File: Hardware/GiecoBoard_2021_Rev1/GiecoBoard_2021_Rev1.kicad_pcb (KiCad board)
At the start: 2 copper layers, 125.7 x 104.1 mm, 62 parts, among them J1 Conn_02x02_Top_Bottom, J10 Test_Point, J11 Conn_02x02_Top_Bottom, J2 Conn_02x02_Top_Bottom, J3 Conn_02x02_Top_Bottom, J4 Conn_02x02_Top_Bottom, J5 Conn_02x02_Top_Bottom, J6 Conn_02x02_Top_Bottom, J7 Conn_02x02_Top_Bottom, J8 Conn_02x02_Top_Bottom, J9 Conn_02x02_Top_Bottom, U1 TM4C129E_Launchpad, U2 LM2576SX-3.3

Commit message: Post CDR update
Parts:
- removed D22: 1n5582, Diode_THT:D_DO-201AD_P15.24mm_Horizontal
- removed G***: LOGO, MRDT_Silkscreens:z_sig_SanfanLiu_sig21.8mmx12.3mm1
- removed G***: LOGO, MRDT_Silkscreens:0_MRDT_Logo_7.5mm
- removed the J10 at (125.1, 88.9)
- removed L1: 100uH, Inductor_SMD:L_0603_1608Metric_Pad1.05x0.95mm_HandSolder
- C1: value 100uF -> 10uF
- C2: value 1000uF -> 10uF; moved to F.Cu
- D1, D11, D13, D14, D16, D3, D4, D6, D8, D9: value LED -> Green
- D10, D12, D15, D17, D18, D19, D2, D20, D5, D7: value LED -> Blue
- D21: value LED -> Green; moved to F.Cu
- R21: moved to F.Cu
- U2: value LM2576SX-3.3 -> OKI; footprint MRDT_Devices:LM2576 -> MRDT_Devices:OKI_Horizontal
- moved D12 74.9 mm to (219.1, 84.1)
- moved D9 74.6 mm to (154.9, 122.8)
- moved D6 43.6 mm to (194.3, 84.1)
- moved D7 42.9 mm to (179.7, 122.8)
- moved D14 42.8 mm to (154.9, 84.1)
- moved D15 42.0 mm to (160.0, 122.8)
- moved D17 42.0 mm to (142.2, 122.8)
- moved D13 39.2 mm to (137.2, 84.1)
- moved D16 38.1 mm to (175.3, 84.1)
- moved D11 22.9 mm to (137.2, 122.8)
- moved D19 19.7 mm to (160.0, 84.1)
- moved D8 19.7 mm to (214.0, 84.1)
- moved D4 19.7 mm to (174.6, 122.8)
- moved D5 19.7 mm to (199.4, 122.8)
- moved D10 14.6 mm to (199.4, 84.1)
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- renumbered J11 to J10, R2 to R1, R7 to R10, R14 to R11, R9 to R12, R16 to R13, R18 to R14, R11 to R15, R20 to R16, R13 to R17, R15 to R18, R17 to R19, R1 to R2, R19 to R20, R4 to R3, R6 to R4, R3 to R5, R8 to R6, R5 to R7, R10 to R8, R12 to R9
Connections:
- C1 pad 1: GND -> Net-(C1-Pad1)
- C1 pad 2: Net-(C1-Pad2) -> GND
- Conn1 pad 2: Net-(C1-Pad2) -> Net-(C1-Pad1)
- R1 pad 1: Net-(D2-Pad2) -> Net-(D1-Pad2)
- R10 pad 1: Net-(D7-Pad2) -> Net-(D10-Pad2)
- R11 pad 1: Net-(D14-Pad2) -> Net-(D11-Pad2)
- R12 pad 1: Net-(D9-Pad2) -> Net-(D12-Pad2)
- R13 pad 1: Net-(D16-Pad2) -> Net-(D13-Pad2)
- R14 pad 1: Net-(D18-Pad2) -> Net-(D14-Pad2)
- R15 pad 1: Net-(D11-Pad2) -> Net-(D15-Pad2)
- R16 pad 1: Net-(D20-Pad2) -> Net-(D16-Pad2)
- R17 pad 1: Net-(D13-Pad2) -> Net-(D17-Pad2)
- R18 pad 1: Net-(D15-Pad2) -> Net-(D18-Pad2)
- R19 pad 1: Net-(D17-Pad2) -> Net-(D19-Pad2)
- R2 pad 1: Net-(D1-Pad2) -> Net-(D2-Pad2)
- R20 pad 1: Net-(D19-Pad2) -> Net-(D20-Pad2)
- R3 pad 1: Net-(D4-Pad2) -> Net-(D3-Pad2)
- R4 pad 1: Net-(D6-Pad2) -> Net-(D4-Pad2)
- R5 pad 1: Net-(D3-Pad2) -> Net-(D5-Pad2)
- R6 pad 1: Net-(D8-Pad2) -> Net-(D6-Pad2)
- R7 pad 1: Net-(D5-Pad2) -> Net-(D7-Pad2)
- R8 pad 1: Net-(D10-Pad2) -> Net-(D8-Pad2)
- R9 pad 1: Net-(D12-Pad2) -> Net-(D9-Pad2)
- U1 pad +5V: Net-(U1-Pad+5V) -> (no net)
- U1 pad PA5: Net-(U1-PadPA5) -> (no net)
- U1 pad PA6: Net-(U1-PadPA6) -> (no net)
- U1 pad PB2: Net-(U1-PadPB2) -> (no net)
- U1 pad PB3: Net-(U1-PadPB3) -> (no net)
- U1 pad PB4: Net-(U1-PadPB4) -> (no net)
- U1 pad PC4: Net-(U1-PadPC4) -> (no net)
- U1 pad PC5: Net-(U1-PadPC5) -> (no net)
- U1 pad PC6: Net-(U1-PadPC6) -> (no net)
- U1 pad PC7: Net-(U1-PadPC7) -> (no net)
- U1 pad PD2: Net-(U1-PadPD2) -> (no net)
- U1 pad PD3: Net-(U1-PadPD3) -> (no net)
- U1 pad PD4: Net-(U1-PadPD4) -> (no net)
- U1 pad PD5: Net-(U1-PadPD5) -> (no net)
- U1 pad PE2: Net-(U1-PadPE2) -> (no net)
- U1 pad PE4: Net-(U1-PadPE4) -> (no net)
- U1 pad PE5: Net-(U1-PadPE5) -> (no net)
- U1 pad PF1: Net-(U1-PadPF1) -> (no net)
- U1 pad PF2: Net-(U1-PadPF2) -> (no net)
- U1 pad PF3: Net-(U1-PadPF3) -> (no net)
- U1 pad PG0: Net-(U1-PadPG0) -> (no net)
- U1 pad PG1: Net-(U1-PadPG1) -> (no net)
- U1 pad PH0: Net-(U1-PadPH0) -> (no net)
- U1 pad PH1: Net-(U1-PadPH1) -> (no net)
- U1 pad PH3: Net-(U1-PadPH3) -> (no net)
- U1 pad PK1: Net-(U1-PadPK1) -> (no net)
- U1 pad PK2: Net-(U1-PadPK2) -> (no net)
- U1 pad PK4: Net-(U1-PadPK4) -> (no net)
- U1 pad PK5: Net-(U1-PadPK5) -> (no net)
- U1 pad PK6: Net-(U1-PadPK6) -> (no net)
- U1 pad PK7: Net-(U1-PadPK7) -> (no net)
- U1 pad PL0: Net-(U1-PadPL0) -> (no net)
- U1 pad PL1: Net-(U1-PadPL1) -> (no net)
- U1 pad PL2: Net-(U1-PadPL2) -> (no net)
- U1 pad PL3: Net-(U1-PadPL3) -> (no net)
- U1 pad PL4: Net-(U1-PadPL4) -> (no net)
- U1 pad PL5: Net-(U1-PadPL5) -> (no net)
- U1 pad PM0: Net-(U1-PadPM0) -> (no net)
- U1 pad PM1: Net-(U1-PadPM1) -> (no net)
- U1 pad PM2: Net-(U1-PadPM2) -> (no net)
- U1 pad PM6: Net-(U1-PadPM6) -> (no net)
- U1 pad PM7: Net-(U1-PadPM7) -> (no net)
- U1 pad PN2: Net-(U1-PadPN2) -> (no net)
- U1 pad PN4: Net-(U1-PadPN4) -> (no net)
- U1 pad PN5: Net-(U1-PadPN5) -> (no net)
- U1 pad PP0: Net-(U1-PadPP0) -> (no net)
- U1 pad PP1: Net-(U1-PadPP1) -> (no net)
- U1 pad PP4: Net-(U1-PadPP4) -> (no net)
- U1 pad PQ0: Net-(U1-PadPQ0) -> (no net)
- U1 pad PQ2: Net-(U1-PadPQ2) -> (no net)
- U1 pad PQ3: Net-(U1-PadPQ3) -> (no net)
- U1 pad Rese: Net-(U1-PadRese) -> (no net)
- U2 pad 1: Net-(C1-Pad2) -> Net-(C1-Pad1)
- U2 pad 2: Net-(D22-Pad1) -> GND
- U2 pad 3: GND -> +3V3
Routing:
- net Net-(C1-Pad1): track 0.00 -> 33.2 mm
- net Net-(D22-Pad1): track 20.1 -> 0.00 mm
- net Net-(C1-Pad2): track 16.9 -> 0.00 mm
- net GND: track 28.4 -> 13.9 mm
- net +3V3: track 0.00 -> 8.25 mm
- net Net-(D6-Pad2): track 3.48 -> 2.70 mm
- net Net-(D14-Pad2): track 3.48 -> 2.70 mm
- net Net-(D13-Pad2): track 3.48 -> 2.70 mm
- net Net-(D8-Pad2): track 3.33 -> 2.70 mm
- net Net-(D20-Pad2): track 3.33 -> 2.70 mm
- net Net-(D19-Pad2): track 3.33 -> 2.70 mm
- net Net-(D18-Pad2): track 3.33 -> 2.70 mm
- net Net-(D16-Pad2): track 3.33 -> 2.70 mm
- net Net-(D12-Pad2): track 3.33 -> 2.70 mm
- net Net-(D10-Pad2): track 3.33 -> 2.70 mm
- removed copper zone on B.Cu, net GND

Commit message: flip tiva and wiring
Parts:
- U1: moved to F.Cu
- moved U1 139.4 mm to (86.4, 112.4), turned to 0 degrees
- moved D12 129.1 mm to (93.1, 55.9), turned to 270 degrees
- moved D2 127.8 mm to (94.1, 96.1), turned to 270 degrees
- moved R12 127.5 mm to (93.1, 60.4), turned to 270 degrees
- moved R2 126.0 mm to (94.1, 101.2), turned to 270 degrees
- moved J5 123.4 mm to (93.4, 49.0)
- moved J1 122.6 mm to (94.0, 86.7)
- moved D8 119.2 mm to (98.1, 55.9), turned to 270 degrees
- moved D1 117.8 mm to (99.2, 96.1), turned to 270 degrees
- moved R8 117.4 mm to (98.1, 60.4), turned to 270 degrees
- moved R1 116.0 mm to (99.2, 101.2), turned to 270 degrees
- moved D10 92.4 mm to (111.3, 56.1), turned to 270 degrees
- moved D5 92.3 mm to (111.1, 95.9), turned to 270 degrees
- moved R10 90.1 mm to (111.3, 60.5), turned to 270 degrees
- moved R5 89.8 mm to (111.1, 101.0), turned to 270 degrees
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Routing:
- net REC_LED_NavigationalControl: track 22.1 -> 9.69 mm
- net REC_LED_ScienceActuation: track 40.2 -> 28.2 mm
- net REC_LED_ScienceSensor: track 26.9 -> 16.1 mm
- net REC_LED_ArmArticulation: track 18.6 -> 8.17 mm
- net REC_LED_PackVoltageDistribution: track 14.5 -> 4.70 mm
- net REC_LED_12VDistribution: track 17.4 -> 8.07 mm
- net REC_LED_Multimedia: track 34.1 -> 26.8 mm
- net REC_LED_BatteryManagement: track 12.3 -> 5.32 mm
- net REC_LED_DriveCommand: track 13.9 -> 7.14 mm
- net REC_LED_Gimbal: track 21.9 -> 15.2 mm
- net Send_NavigationalControl: track 43.2 -> 40.3 mm
- net Send_Multimedia: track 50.0 -> 52.8 mm
- net Send_ScienceActuation: track 57.0 -> 55.4 mm
- net Send_12VDistribution: track 36.3 -> 37.5 mm
- net Send_Gimbal: track 38.4 -> 39.5 mm
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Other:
- board size 125.7 x 104.1 mm -> 125.1 x 106.8 mm

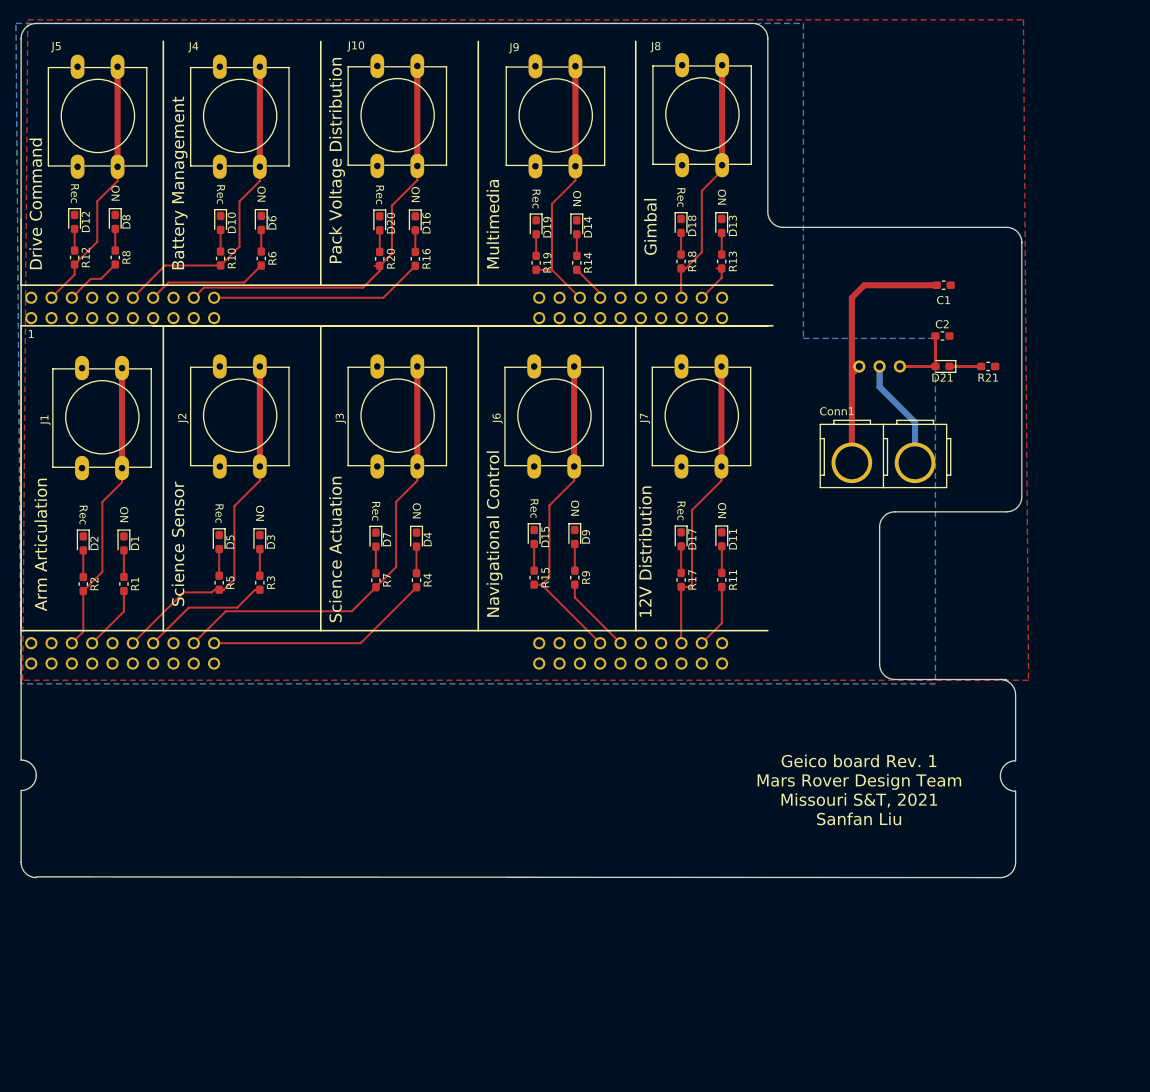
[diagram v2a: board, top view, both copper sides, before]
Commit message: board changes fixed
-edge cuts corrected
-andersons changed to horizontal andersons
-3v3 plane moved where necessary
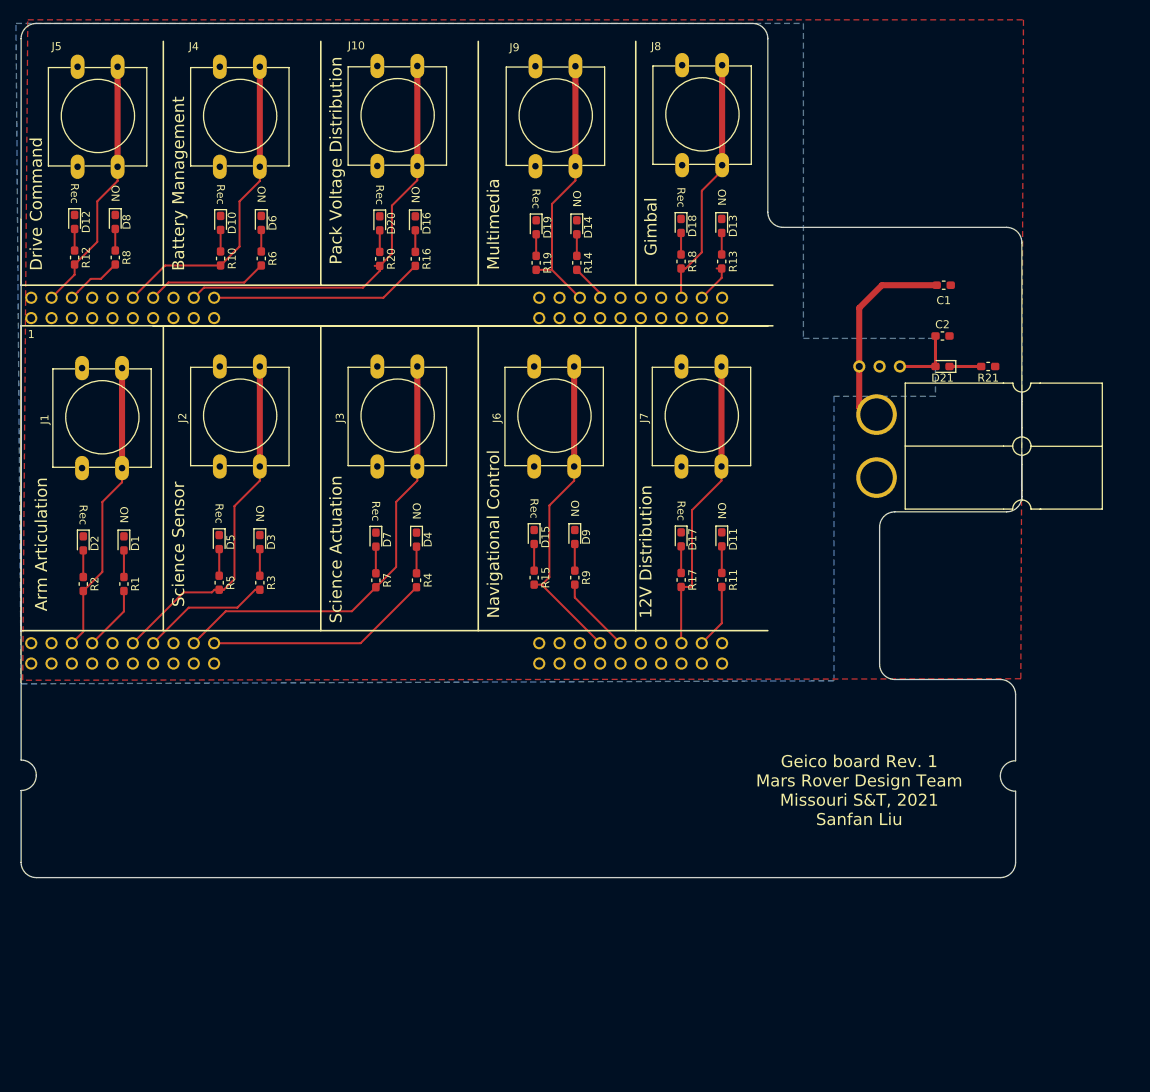
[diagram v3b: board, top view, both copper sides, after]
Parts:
- Conn1: footprint MRDT_Connectors:Anderson_2_Vertical_Sidy_by_Side -> MRDT_Connectors:Anderson_2_Horizontal_Side_by_Side
- moved Conn1 5.14 mm to (193.3, 87.9)
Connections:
- U1 pad +5V: (no net) -> Net-(U1-Pad+5V)
- U1 pad PA5: (no net) -> Net-(U1-PadPA5)
- U1 pad PA6: (no net) -> Net-(U1-PadPA6)
- U1 pad PB2: (no net) -> Net-(U1-PadPB2)
- U1 pad PB3: (no net) -> Net-(U1-PadPB3)
- U1 pad PB4: (no net) -> Net-(U1-PadPB4)
- U1 pad PC4: (no net) -> Net-(U1-PadPC4)
- U1 pad PC5: (no net) -> Net-(U1-PadPC5)
- U1 pad PC6: (no net) -> Net-(U1-PadPC6)
- U1 pad PC7: (no net) -> Net-(U1-PadPC7)
- U1 pad PD2: (no net) -> Net-(U1-PadPD2)
- U1 pad PD3: (no net) -> Net-(U1-PadPD3)
- U1 pad PD4: (no net) -> Net-(U1-PadPD4)
- U1 pad PD5: (no net) -> Net-(U1-PadPD5)
- U1 pad PE2: (no net) -> Net-(U1-PadPE2)
- U1 pad PE4: (no net) -> Net-(U1-PadPE4)
- U1 pad PE5: (no net) -> Net-(U1-PadPE5)
- U1 pad PF1: (no net) -> Net-(U1-PadPF1)
- U1 pad PF2: (no net) -> Net-(U1-PadPF2)
- U1 pad PF3: (no net) -> Net-(U1-PadPF3)
- U1 pad PG0: (no net) -> Net-(U1-PadPG0)
- U1 pad PG1: (no net) -> Net-(U1-PadPG1)
- U1 pad PH0: (no net) -> Net-(U1-PadPH0)
- U1 pad PH1: (no net) -> Net-(U1-PadPH1)
- U1 pad PH3: (no net) -> Net-(U1-PadPH3)
- U1 pad PK1: (no net) -> Net-(U1-PadPK1)
- U1 pad PK2: (no net) -> Net-(U1-PadPK2)
- U1 pad PK4: (no net) -> Net-(U1-PadPK4)
- U1 pad PK5: (no net) -> Net-(U1-PadPK5)
- U1 pad PK6: (no net) -> Net-(U1-PadPK6)
- U1 pad PK7: (no net) -> Net-(U1-PadPK7)
- U1 pad PL0: (no net) -> Net-(U1-PadPL0)
- U1 pad PL1: (no net) -> Net-(U1-PadPL1)
- U1 pad PL2: (no net) -> Net-(U1-PadPL2)
- U1 pad PL3: (no net) -> Net-(U1-PadPL3)
- U1 pad PL4: (no net) -> Net-(U1-PadPL4)
- U1 pad PL5: (no net) -> Net-(U1-PadPL5)
- U1 pad PM0: (no net) -> Net-(U1-PadPM0)
- U1 pad PM1: (no net) -> Net-(U1-PadPM1)
- U1 pad PM2: (no net) -> Net-(U1-PadPM2)
- U1 pad PM6: (no net) -> Net-(U1-PadPM6)
- U1 pad PM7: (no net) -> Net-(U1-PadPM7)
- U1 pad PN2: (no net) -> Net-(U1-PadPN2)
- U1 pad PN4: (no net) -> Net-(U1-PadPN4)
- U1 pad PN5: (no net) -> Net-(U1-PadPN5)
- U1 pad PP0: (no net) -> Net-(U1-PadPP0)
- U1 pad PP1: (no net) -> Net-(U1-PadPP1)
- U1 pad PP4: (no net) -> Net-(U1-PadPP4)
- U1 pad PQ0: (no net) -> Net-(U1-PadPQ0)
- U1 pad PQ2: (no net) -> Net-(U1-PadPQ2)
- U1 pad PQ3: (no net) -> Net-(U1-PadPQ3)
- U1 pad Rese: (no net) -> Net-(U1-PadRese)
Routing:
- net GND: track 13.9 -> 0.00 mm
- net Net-(C1-Pad1): track 33.2 -> 26.0 mm
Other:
- outline, holes or cut-outs redrawn
